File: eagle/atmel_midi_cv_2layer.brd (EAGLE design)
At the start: 98.7 x 49.5 mm, 52 parts, among them IC2 TL072P, Q1 16M, U1 ATMEGA328P_PDIP, U2 TLV2372IP

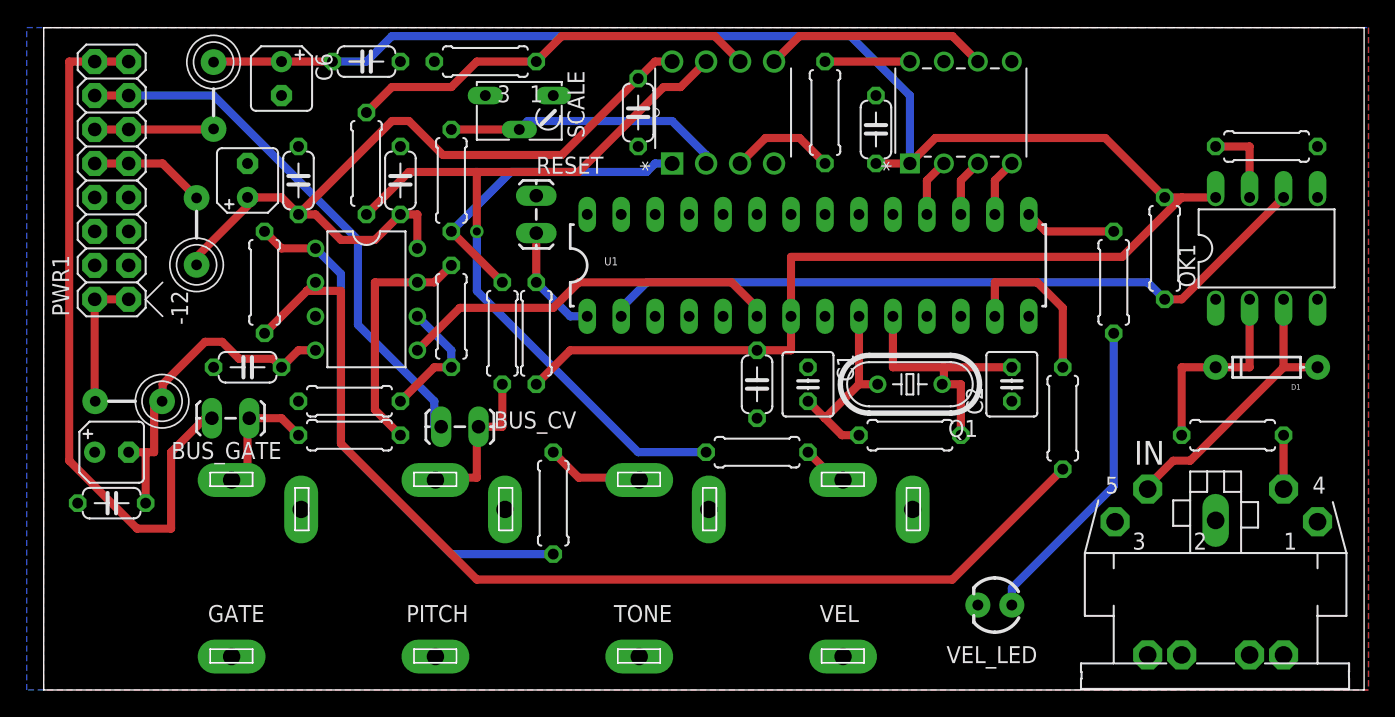
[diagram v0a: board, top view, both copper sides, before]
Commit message: ICSP added and rerouted
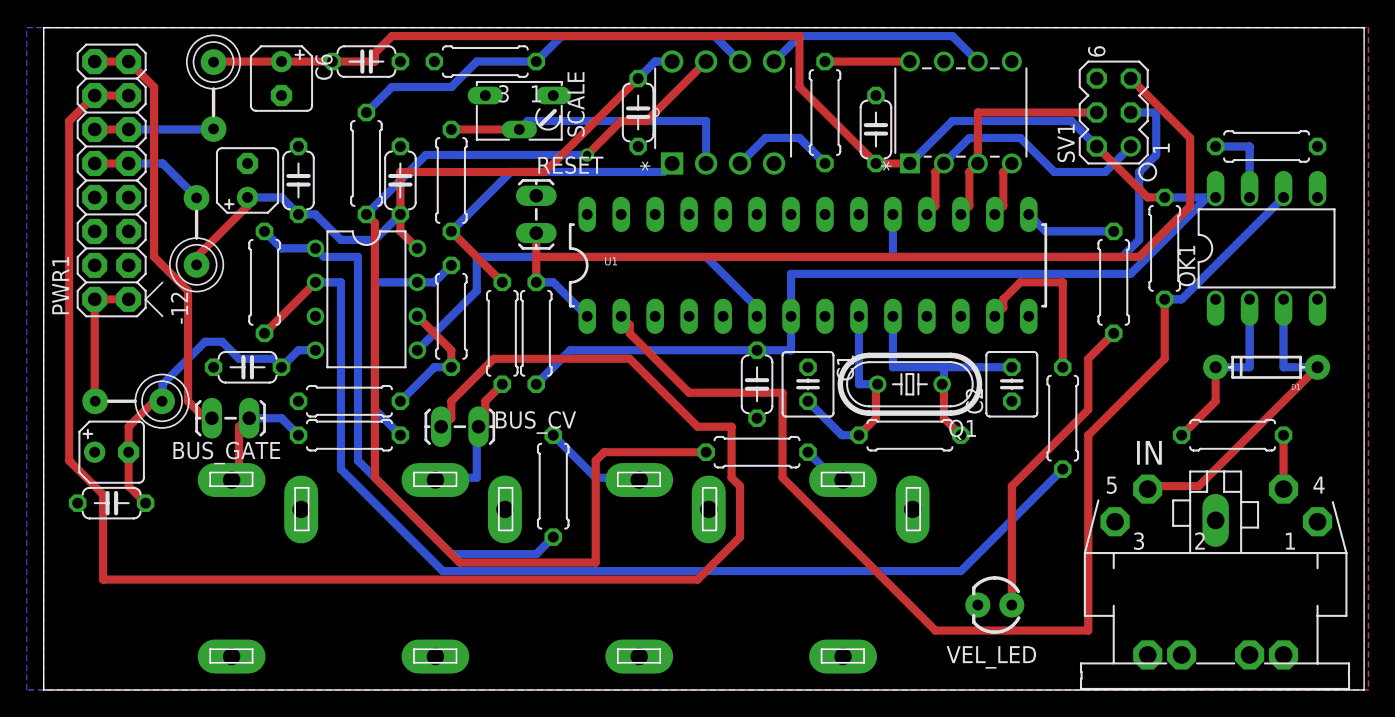
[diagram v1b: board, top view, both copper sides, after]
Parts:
- added SV1: (no value), con-lstb:MA03-2
- moved R4 1.27 mm to (38.1, 15.2)
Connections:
- new net N$2: SV1.3, U1.19
- net +5V: now also SV1.2
- net GND: now also SV1.6
- net N$25: now also SV1.4
- net N$43: now also SV1.5
- net N$45: now also SV1.1
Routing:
- net N$15: track 41.0 -> 124.7 mm
- net N$43: track 8.55 -> 70.4 mm
- net N$2: track 0.00 -> 34.1 mm
- net N$30: track 54.6 -> 87.9 mm
- net N$39: track 61.2 -> 85.4 mm
- net N$1: track 53.8 -> 32.1 mm
- net N$45: track 4.34 -> 20.9 mm
- net N$25: track 4.34 -> 17.0 mm
- net +12V: track 59.0 -> 50.1 mm
- net N$22: track 28.9 -> 32.0 mm
- net N$33: track 21.7 -> 24.2 mm
- net N$35: track 39.0 -> 41.0 mm
- net N$37: track 21.0 -> 22.5 mm
- net N$7: track 15.2 -> 13.8 mm
- net N$4: track 14.9 -> 15.8 mm
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
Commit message: updated power with shroud
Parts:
- moved C10 3.81 mm to (5.08, 14.0)
- moved C11 3.81 mm to (5.08, 10.2)
- moved U$3 2.84 mm to (5.08, 19.1)
- moved PWR1 2.54 mm to (5.08, 33.0)
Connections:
- net N$37: now also SCALE.P$1
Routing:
- net -12V: track 24.9 -> 30.0 mm
- net N$37: track 22.5 -> 25.0 mm
- net N$34: track 8.93 -> 9.98 mm
- net N$11: track 8.71 -> 7.66 mm
- net N$17: track 10.2 -> 11.0 mm
- net N$15: track 124.7 -> 125.4 mm
- net N$1: track 32.1 -> 32.7 mm

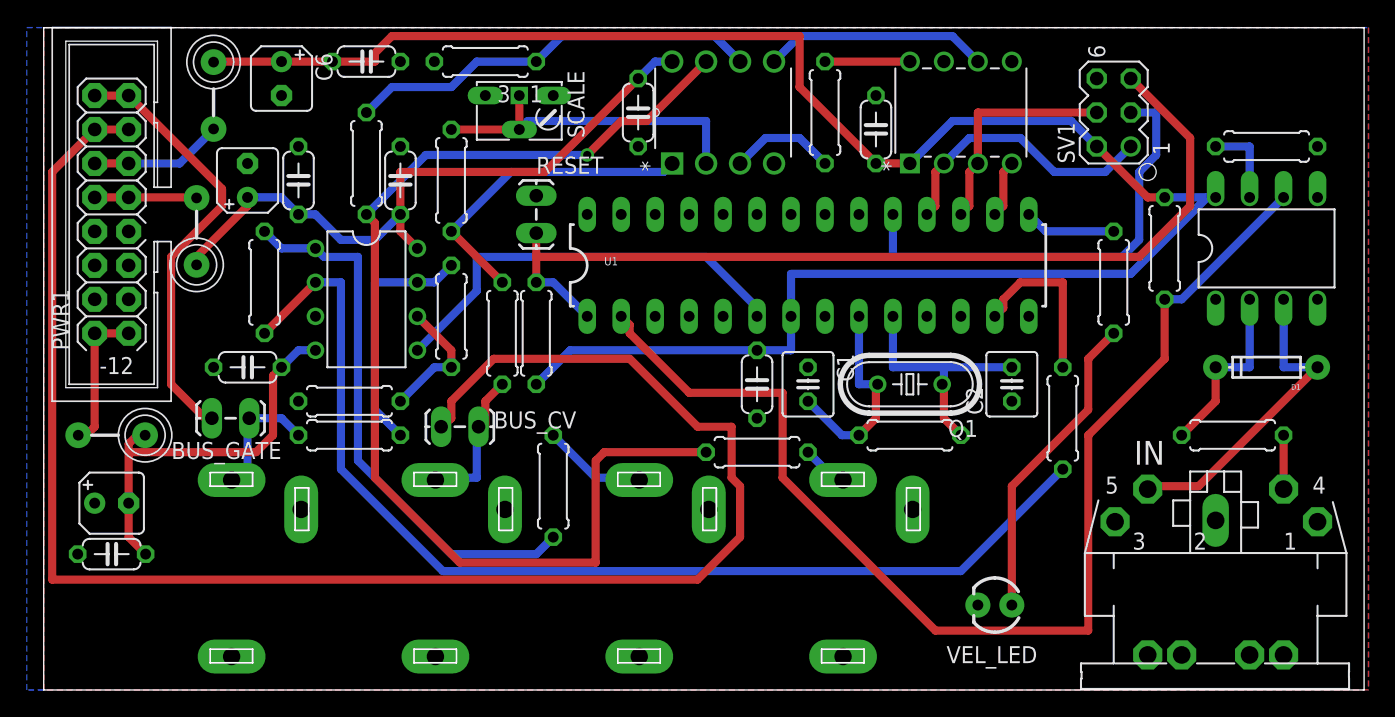
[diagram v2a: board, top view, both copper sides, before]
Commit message: route better clearance for midi resistor and scale pot
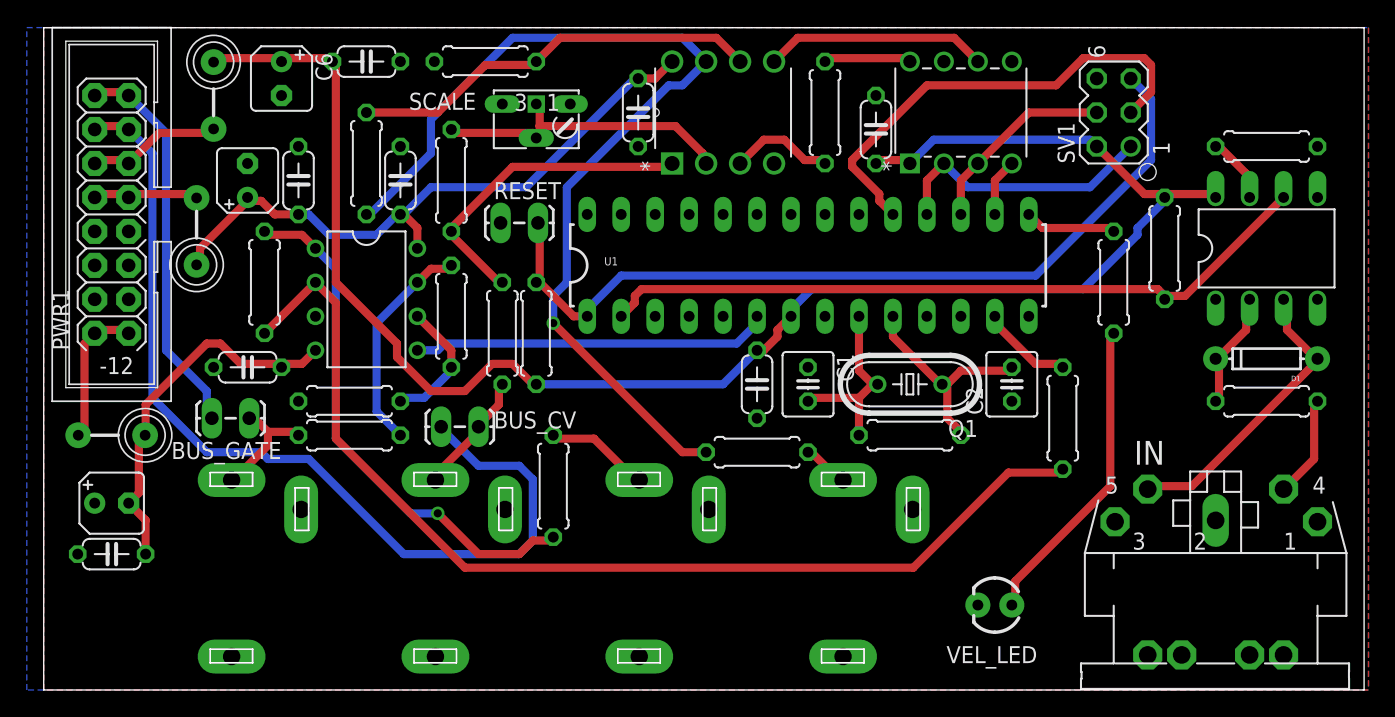
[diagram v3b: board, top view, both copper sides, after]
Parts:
- moved R16 3.59 mm to (91.4, 21.6)
- moved SCALE 1.42 mm to (36.8, 43.8)
- moved D1 0.64 mm to (91.4, 24.8)
- moved RESET 0.63 mm to (36.8, 34.9), turned to 180 degrees
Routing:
- net N$15: track 125.4 -> 70.4 mm
- net N$30: track 87.9 -> 54.2 mm
- net +5V: track 145.3 -> 128.8 mm
- net N$39: track 85.4 -> 73.4 mm
- net N$43: track 70.4 -> 63.4 mm
- net N$21: track 12.9 -> 7.10 mm
- net N$22: track 32.0 -> 26.7 mm
- net N$7: track 13.8 -> 8.91 mm
- net N$8: track 4.03 -> 7.63 mm
- net N$1: track 32.7 -> 29.7 mm
- net N$28: track 81.6 -> 79.3 mm
- net N$25: track 17.0 -> 14.8 mm
- net +12V: track 50.1 -> 48.0 mm
- net N$5: track 18.6 -> 16.6 mm
- net N$33: track 24.2 -> 22.3 mm
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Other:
- board text added: "Release v0.6"
- board text removed: "Release v0.5"

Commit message: label tweaks and power filter moved
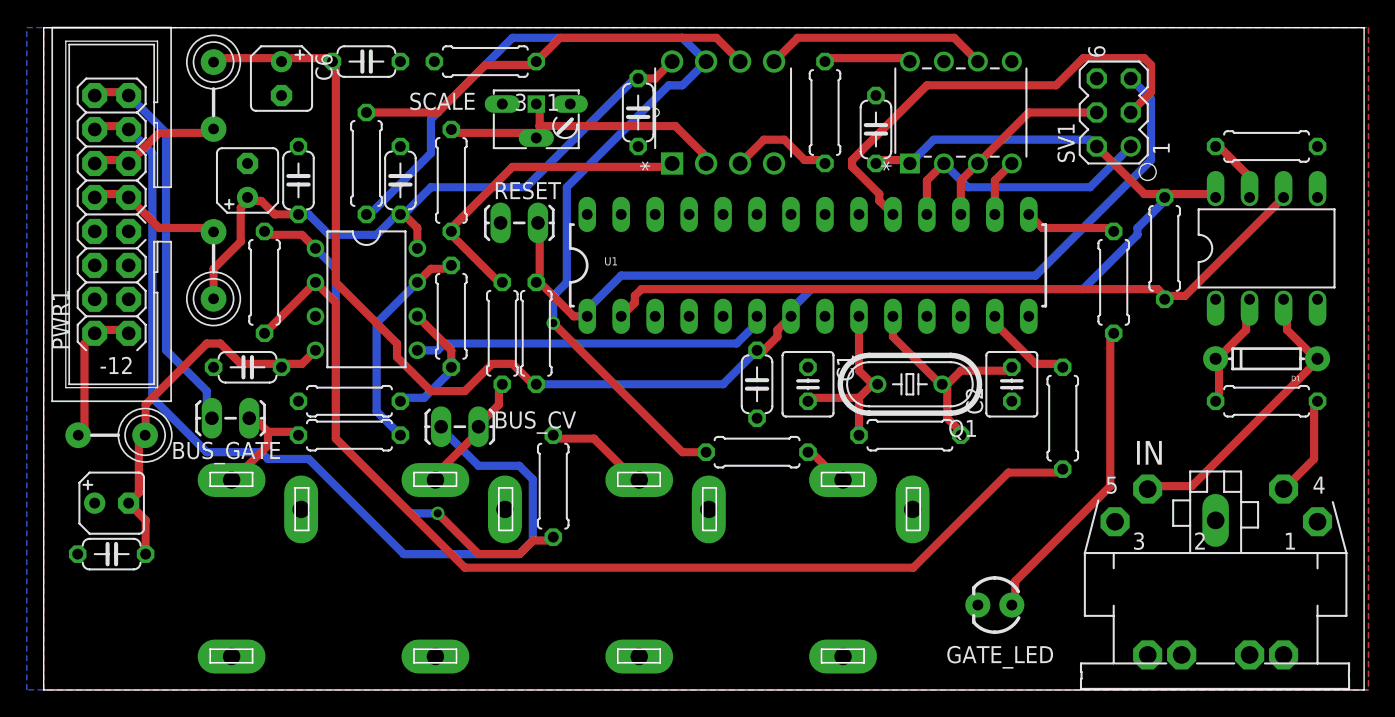
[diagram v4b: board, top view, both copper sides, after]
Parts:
- moved U$2 2.84 mm to (12.7, 31.8)
- renumbered VEL_LED to GATE_LED
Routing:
- net N$11: track 8.07 -> 10.3 mm
- net +12V: track 48.0 -> 50.0 mm
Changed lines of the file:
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@@
 <layer number="27" name="tValues" color="7" fill="1" visible="yes" active="yes"/>
 <layer number="28" name="bValues" color="7" fill="1" visible="yes" active="yes"/>
-<layer number="29" name="tStop" color="7" fill="3" visible="no" active="yes"/>
-<layer number="30" name="bStop" color="7" fill="6" visible="no" active="yes"/>
-<layer number="31" name="tCream" color="7" fill="4" visible="no" active="yes"/>
-<layer number="32" name="bCream" color="7" fill="5" visible="no" active="yes"/>
-<layer number="33" name="tFinish" color="6" fill="3" visible="no" active="yes"/>
-<layer number="34" name="bFinish" color="6" fill="6" visible="no" active="yes"/>
-<layer number="35" name="tGlue" color="7" fill="4" visible="no" active="yes"/>
-<layer number="36" name="bGlue" color="7" fill="5" visible="no" active="yes"/>
-<layer number="37" name="tTest" color="7" fill="1" visible="no" active="yes"/>
-<layer number="38" name="bTest" color="7" fill="1" visible="no" active="yes"/>
+<layer number="29" name="tStop" color="7" fill="3" visible="yes" active="yes"/>
+<layer number="30" name="bStop" color="7" fill="6" visible="yes" active="yes"/>
+<layer number="31" name="tCream" color="7" fill="4" visible="yes" active="yes"/>
+<layer number="32" name="bCream" color="7" fill="5" visible="yes" active="yes"/>
+<layer number="33" name="tFinish" color="6" fill="3" visible="yes" active="yes"/>
+<layer number="34" name="bFinish" color="6" fill="6" visible="yes" active="yes"/>
+<layer number="35" name="tGlue" color="7" fill="4" visible="yes" active="yes"/>
+<layer number="36" name="bGlue" color="7" fill="5" visible="yes" active="yes"/>
+<layer number="37" name="tTest" color="7" fill="1" visible="yes" active="yes"/>
+<layer number="38" name="bTest" color="7" fill="1" visible="yes" active="yes"/>
 <layer number="39" name="tKeepout" color="4" fill="11" visible="yes" active="yes"/>
 <layer number="40" name="bKeepout" color="1" fill="11" visible="yes" active="yes"/>
@@
 <layer number="42" name="bRestrict" color="1" fill="10" visible="yes" active="yes"/>
 <layer number="43" name="vRestrict" color="2" fill="10" visible="yes" active="yes"/>
-<layer number="44" name="Drills" color="7" fill="1" visible="no" active="yes"/>
-<layer number="45" name="Holes" color="7" fill="1" visible="no" active="yes"/>
+<layer number="44" name="Drills" color="7" fill="1" visible="yes" active="yes"/>
+<layer number="45" name="Holes" color="7" fill="1" visible="yes" active="yes"/>
 <layer number="46" name="Milling" color="3" fill="1" visible="yes" active="yes"/>
-<layer number="47" name="Measures" color="7" fill="1" visible="no" active="yes"/>
+<layer number="47" name="Measures" color="7" fill="1" visible="yes" active="yes"/>
 <layer number="48" name="Document" color="7" fill="1" visible="yes" active="yes"/>
 <layer number="49" name="Reference" color="7" fill="1" visible="yes" active="yes"/>
@@
 <wire x1="98.73" y1="49.52" x2="0" y2="49.52" width="0" layer="20"/>
 <wire x1="0" y1="49.52" x2="0" y2="0" width="0" layer="20"/>
-<text x="64.77" y="6.985" size="1.6764" layer="26" rot="MR0">https://github.com/jbeuckm/atmega_midi_cv_basic</text>
+<text x="67.31" y="6.985" size="1.6764" layer="26" rot="MR0">https://github.com/jbeuckm/atmega_midi_cv_basic</text>
 <text x="25.4" y="9.525" size="1.778" layer="26" rot="MR0">Release v0.6</text>
 <circle x="82.55" y="38.735" radius="0.635" width="0.1016" layer="21"/>
@@
 </element>
 <element name="C5" library="rcl" package="B45181A" value="10u" x="15.24" y="38.1" smashed="yes" rot="R90">
-<attribute name="VALUE" x="10.033" y="38.989" size="1.27" layer="27" ratio="10"/>
+<attribute name="VALUE" x="12.446" y="36.703" size="1.27" layer="27" ratio="10" rot="R90"/>
 </element>
 <element name="C6" library="rcl" package="B45181A" value="10u" x="17.78" y="45.72" smashed="yes" rot="R270">
@@
 <element name="D1" library="SparkFun-DiscreteSemi" package="DIODE-1N4148" value="" x="91.44" y="24.765" rot="R180"/>
 <element name="GATE" library="erthenvar" package="JACK-90DEG-ITEAD" value="AUDIO-JACKITEAD" x="19.05" y="0" smashed="yes" rot="R180">
-<attribute name="NAME" x="7.62" y="1.27" size="1.27" layer="22" rot="MR90"/>
+<attribute name="NAME" x="7.62" y="0.635" size="1.27" layer="22" rot="MR90"/>
 </element>
 <element name="BUS_GATE" library="SparkFun-Connectors" package="1X02_LOCK_LONGPADS" value="M02LOCK_LONGPADS" x="15.24" y="20.32" smashed="yes" rot="R180">
@@
 </element>
 <element name="IC2" library="linear" package="DIL08" value="TL072P" x="24.13" y="29.21" smashed="yes" rot="R270">
-<attribute name="VALUE" x="23.495" y="30.226" size="1.27" layer="27" ratio="10" rot="R270"/>
+<attribute name="VALUE" x="23.495" y="32.131" size="1.27" layer="27" ratio="10" rot="R270"/>
 </element>
 <element name="IN" library="adafruit" package="CP-2350" value="MIDIJACK" x="87.63" y="0"/>
@@
 <attribute name="OC_FARNELL" value="9860150" x="91.44" y="33.02" size="1.778" layer="27" display="off"/>
 <attribute name="OC_NEWARK" value="35K5294" x="91.44" y="33.02" size="1.778" layer="27" display="off"/>
-<attribute name="VALUE" x="87.884" y="32.385" size="1.27" layer="27" ratio="10"/>
+<attribute name="VALUE" x="89.154" y="32.385" size="1.27" layer="27" ratio="10"/>
 </element>
 <element name="PITCH" library="erthenvar" package="JACK-90DEG-ITEAD" value="AUDIO-JACKITEAD" x="34.29" y="0" smashed="yes" rot="R180">
-<attribute name="NAME" x="22.86" y="1.27" size="1.27" layer="22" rot="MR90"/>
+<attribute name="NAME" x="22.86" y="0.635" size="1.27" layer="22" rot="MR90"/>
 </element>
 <element name="PWR1" library="eurorack" package="POWER_16" value="POWER" x="5.08" y="33.02" smashed="yes" rot="R90">
@@
 </element>
 <element name="TONE" library="erthenvar" package="JACK-90DEG-ITEAD" value="AUDIO-JACKITEAD" x="49.53" y="0" smashed="yes" rot="R180">
-<attribute name="NAME" x="38.1" y="1.27" size="1.27" layer="22" rot="MR90"/>
+<attribute name="NAME" x="38.1" y="0.635" size="1.27" layer="22" rot="MR90"/>
 </element>
 <element name="U$1" library="adafruit" package="FB" value="FB" x="12.7" y="44.45" smashed="yes" rot="R90"/>
-<element name="U$2" library="adafruit" package="FB" value="FB" x="11.43" y="34.29" smashed="yes" rot="R270"/>
+<element name="U$2" library="adafruit" package="FB" value="FB" x="12.7" y="31.75" smashed="yes" rot="R270"/>
 <element name="U$3" library="adafruit" package="FB" value="FB" x="5.08" y="19.05" smashed="yes"/>
 <element name="U$4" library="MCP4822" package="DIP254P762X432-8" value="MCP4822-E/P" x="72.39" y="46.99" smashed="yes" rot="R90">
@@
 <attribute name="PACKAGE" value="PDIP" x="54.61" y="46.99" size="1.778" layer="27" rot="R90" display="off"/>
 <attribute name="SUPPLIER" value="Texas Instruments" x="54.61" y="46.99" size="1.778" layer="27" rot="R90" display="off"/>
-<attribute name="VALUE" x="46.1772" y="41.402" size="1.4224" layer="27" ratio="10" rot="SR0"/>
+<attribute name="VALUE" x="46.1772" y="42.037" size="1.4224" layer="27" ratio="10" rot="SR0"/>
 </element>
 <element name="VEL" library="erthenvar" package="JACK-90DEG-ITEAD" value="AUDIO-JACKITEAD" x="64.77" y="0" smashed="yes" rot="R180">
-<attribute name="NAME" x="53.34" y="1.27" size="1.27" layer="22" rot="MR90"/>
-</element>
-<element name="VEL_LED" library="SparkFun-LED" package="LED3MM" value="" x="71.12" y="6.35" smashed="yes" rot="R180">
-<attribute name="NAME" x="74.295" y="3.2766" size="1.27" layer="25" ratio="10" rot="R180"/>
+<attribute name="NAME" x="53.34" y="0.635" size="1.27" layer="22" rot="MR90"/>
+</element>
+<element name="GATE_LED" library="SparkFun-LED" package="LED3MM" value="" x="71.12" y="6.35" smashed="yes" rot="R180">
+<attribute name="NAME" x="75.565" y="3.2766" size="1.27" layer="25" ratio="10" rot="R180"/>
 <attribute name="VALUE" x="67.9196" y="8.1534" size="1.27" layer="27" ratio="10" rot="R180"/>
 </element>
@@
 <wire x1="16.256" y1="36.576" x2="17.272" y2="35.56" width="0.6096" layer="1"/>
 <wire x1="15.24" y1="36.576" x2="16.256" y2="36.576" width="0.6096" layer="1"/>
-<wire x1="11.684" y1="33.02" x2="11.684" y2="32.004" width="0.6096" layer="1"/>
-<wire x1="15.24" y1="36.576" x2="11.684" y2="33.02" width="0.6096" layer="1"/>
-<wire x1="11.684" y1="32.004" x2="11.43" y2="31.79" width="0.6096" layer="1"/>
+<wire x1="12.7" y1="31.496" x2="12.7" y2="29.25" width="0.6096" layer="1"/>
+<wire x1="14.732" y1="33.528" x2="12.7" y2="31.496" width="0.6096" layer="1"/>
+<wire x1="14.732" y1="36.068" x2="14.732" y2="33.528" width="0.6096" layer="1"/>
+<wire x1="15.24" y1="36.576" x2="14.732" y2="36.068" width="0.6096" layer="1"/>
 <wire x1="15.24" y1="36.576" x2="15.24" y2="36.83" width="0.6096" layer="1"/>
 <wire x1="24.892" y1="34.036" x2="26.416" y2="35.56" width="0.6096" layer="16"/>
@@
 <wire x1="4.064" y1="37.084" x2="3.81" y2="36.83" width="0.6096" layer="1"/>
 <wire x1="6.096" y1="37.084" x2="6.35" y2="36.83" width="0.6096" layer="1"/>
-<wire x1="6.604" y1="37.084" x2="11.176" y2="37.084" width="0.6096" layer="1"/>
-<wire x1="11.176" y1="37.084" x2="11.43" y2="36.79" width="0.6096" layer="1"/>
-<wire x1="6.604" y1="37.084" x2="6.35" y2="36.83" width="0.6096" layer="1"/>
+<wire x1="8.636" y1="34.544" x2="12.7" y2="34.544" width="0.6096" layer="1"/>
+<wire x1="6.35" y1="36.83" x2="8.636" y2="34.544" width="0.6096" layer="1"/>
+<wire x1="12.7" y1="34.544" x2="12.7" y2="34.25" width="0.6096" layer="1"/>
 </signal>
 <signal name="N$22">
@@
 </signal>
 <signal name="N$18">
-<contactref element="VEL_LED" pad="A"/>
+<contactref element="GATE_LED" pad="A"/>
 <contactref element="R25" pad="1"/>
 <wire x1="79.756" y1="15.24" x2="79.756" y2="26.416" width="0.6096" layer="1"/>
@@
 </signal>
 <signal name="GND">
-<contactref element="VEL_LED" pad="K"/>
+<contactref element="GATE_LED" pad="K"/>
 <contactref element="IC2" pad="3"/>
 <contactref element="C9" pad="2"/>
